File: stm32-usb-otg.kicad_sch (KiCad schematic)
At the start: 42 parts

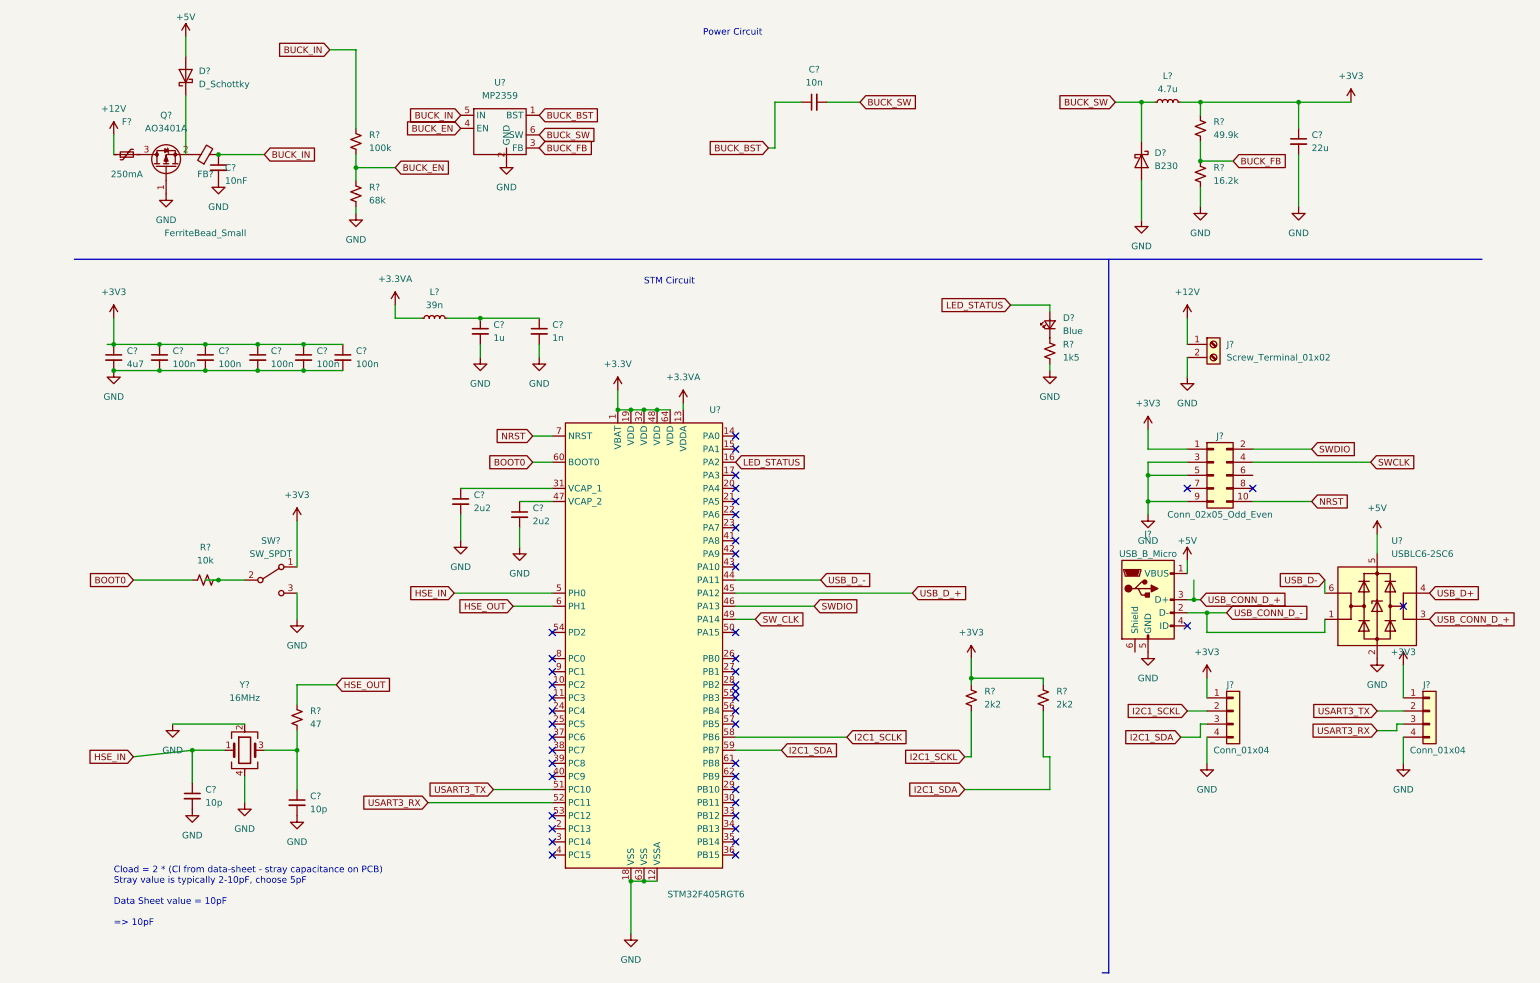
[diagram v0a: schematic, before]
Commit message: Resolving a few ERC errors with power flag based power.
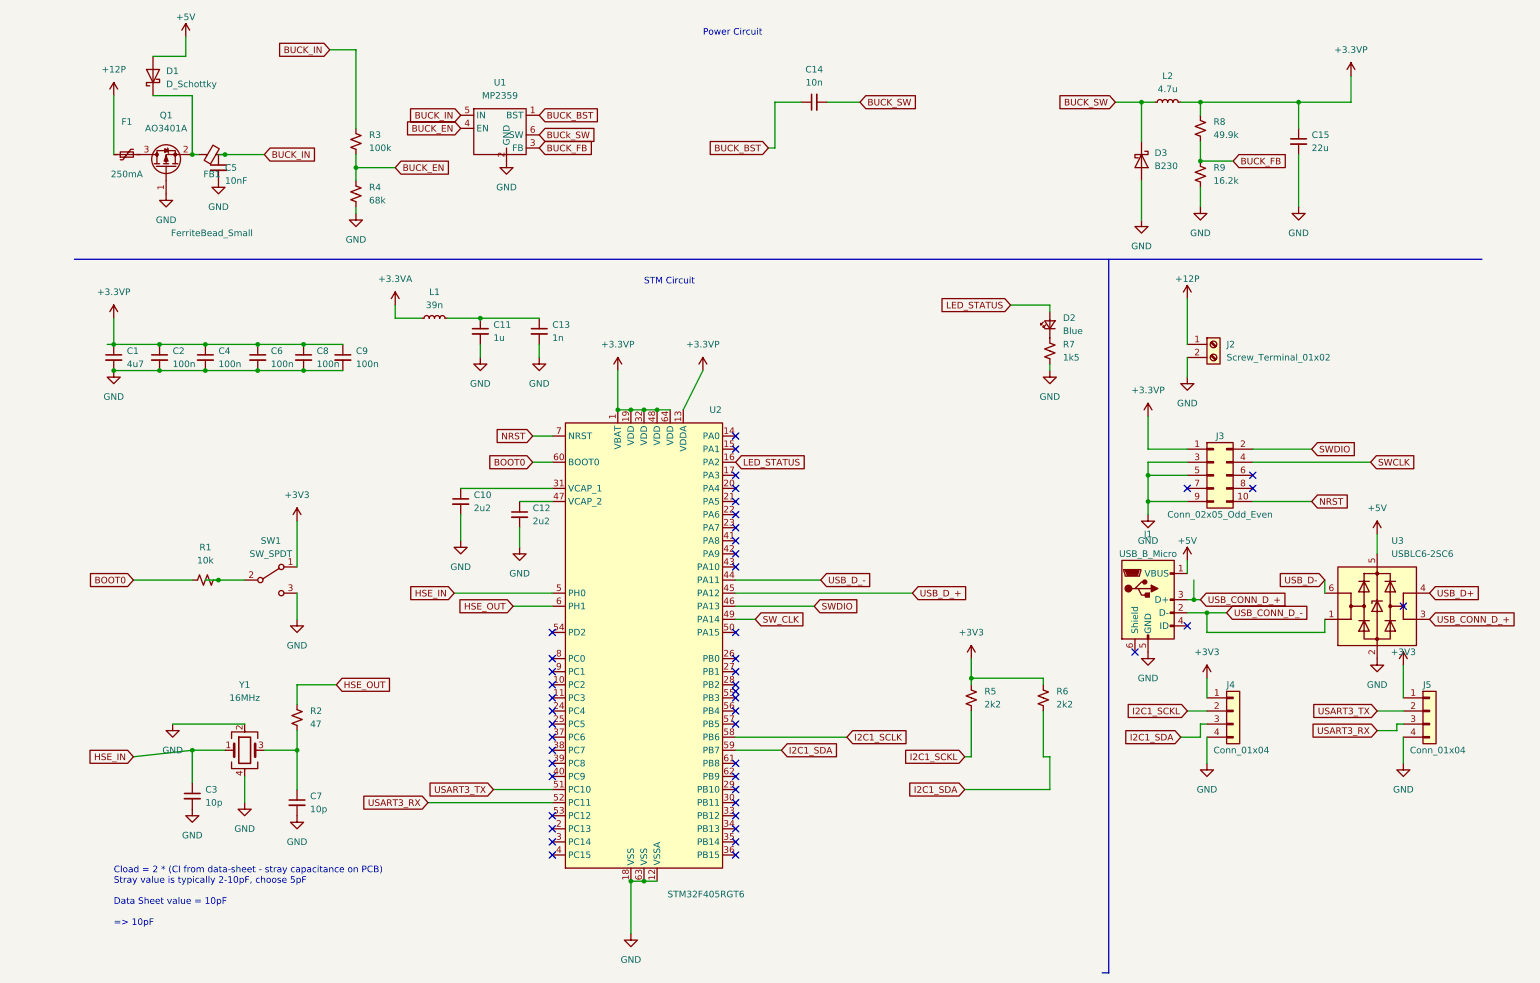
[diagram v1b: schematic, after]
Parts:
- removed D?: D_Schottky, symbol Device:D_Schottky
- added D1: D_Schottky, symbol Device:D_Schottky
- C1: renamed from C?; footprint (none) -> Capacitor_SMD:CP_Elec_3x5.3
- gave numbers to parts that had none: 40
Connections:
- net +3.3VA: no longer U2.13 (VDDA)
- net +3V3: no longer C1.1, C15.1, C2.1, C4.1, C6.1, C8.1, C9.1, J3.1 (Pin_1), L2.2, R8.1, U2.1 (VBAT), U2.19 (VDD), U2.32 (VDD), U2.48 (VDD), U2.64 (VDD)
- net +5V: now also D1.2 (A)
- net at FB1.1, Q1.2 (S): now also D1.1 (K)
- net +12V renamed +12P
- new net +3.3VP: C1.1, C15.1, C2.1, C4.1, C6.1, C8.1, C9.1, J3.1 (Pin_1), L2.2, R8.1, U2.1 (VBAT), U2.13 (VDDA), U2.19 (VDD), U2.32 (VDD), U2.48 (VDD), U2.64 (VDD)
- no-connect marks 45 -> 47
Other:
- moved on the sheet: FB1

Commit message: Solving a few ERC errors.
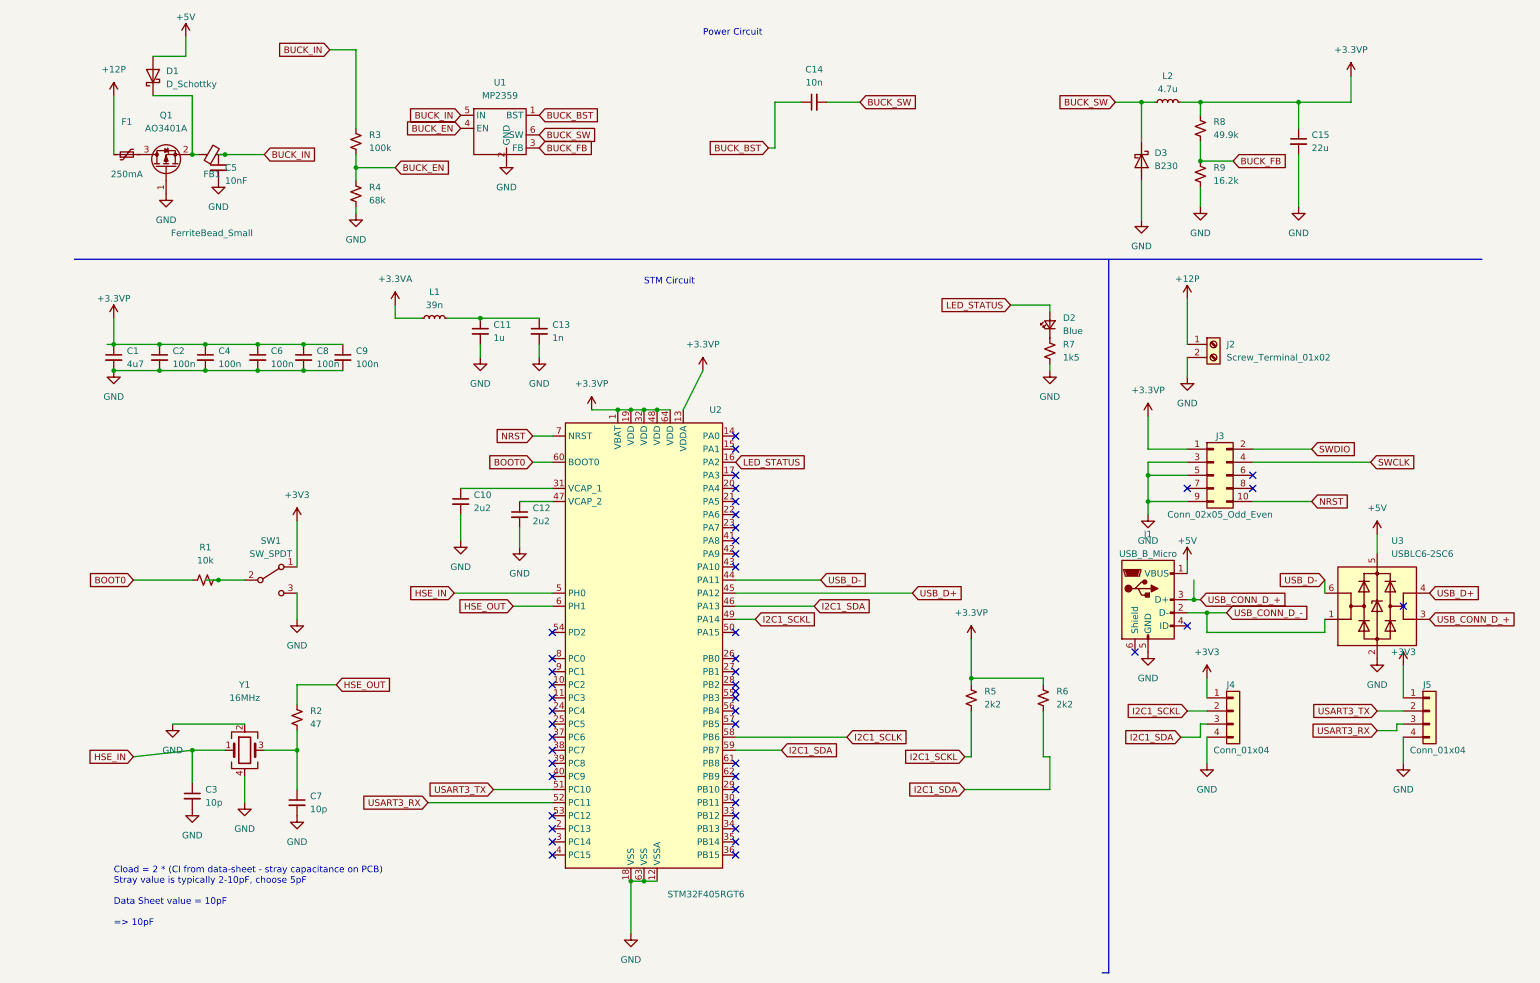
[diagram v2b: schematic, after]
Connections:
- net BUCk_SW is gone; now on net BUCK_SW: U1.6 (SW)
- net SW_CLK is gone; now on net I2C1_SCKL: U2.49 (PA14)
- net USB_D_+ is gone; now on net USB_D+: U2.45 (PA12)
- net USB_D_- is gone; now on net USB_D-: U2.44 (PA11)
- net +3.3VP: now also R5.1, R6.1
- net +3V3: no longer R5.1, R6.1
- net I2C1_SDA: now also U2.46 (PA13)
- net SWDIO: no longer U2.46 (PA13)
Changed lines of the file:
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@@
   (junction (at 231.14 40.64) (diameter 0) (color 0 0 0 0)
   )
+  (junction (at 123.19 88.9) (diameter 0) (color 0 0 0 0)
+  )
+  (junction (at 231.14 29.21) (diameter 0) (color 0 0 0 0)
+  )
+  (junction (at 220.98 106.68) (diameter 0) (color 0 0 0 0)
+  )
+  (junction (at 29.21 81.28) (diameter 0) (color 0 0 0 0)
+  )
   (junction (at 125.73 88.9) (diameter 0) (color 0 0 0 0)
   )
-  (junction (at 231.14 29.21) (diameter 0) (color 0 0 0 0)
-  )
-  (junction (at 220.98 106.68) (diameter 0) (color 0 0 0 0)
-  )
-  (junction (at 29.21 81.28) (diameter 0) (color 0 0 0 0)
-  )
   (junction (at 35.56 39.37) (diameter 0) (color 0 0 0 0)
   )
@@
   (junction (at 123.19 180.34) (diameter 0) (color 0 0 0 0)
   )
+  (junction (at 118.11 88.9) (diameter 0) (color 0 0 0 0)
+  )
   (junction (at 232.41 128.27) (diameter 0) (color 0 0 0 0)
   )
-  (junction (at 118.11 88.9) (diameter 0) (color 0 0 0 0)
-  )
   (junction (at 120.65 88.9) (diameter 0) (color 0 0 0 0)
   )
   (junction (at 186.69 140.97) (diameter 0) (color 0 0 0 0)
-  )
-  (junction (at 123.19 88.9) (diameter 0) (color 0 0 0 0)
   )
   (junction (at 35.56 154.94) (diameter 0) (color 0 0 0 0)
@@
     (stroke (width 0) (type default) (color 0 0 0 0))
   )
+  (wire (pts (xy 125.73 88.9) (xy 128.27 88.9))
+    (stroke (width 0) (type default) (color 0 0 0 0))
+  )
   (wire (pts (xy 232.41 152.4) (xy 232.41 157.48))
     (stroke (width 0) (type default) (color 0 0 0 0))
   )
-  (wire (pts (xy 118.11 81.28) (xy 118.11 88.9))
-    (stroke (width 0) (type default) (color 0 0 0 0))
-  )
   (wire (pts (xy 158.75 29.21) (xy 165.1 29.21))
     (stroke (width 0) (type default) (color 0 0 0 0))
@@
     (stroke (width 0) (type default) (color 0 0 0 0))
   )
+  (wire (pts (xy 113.03 88.9) (xy 118.11 88.9))
+    (stroke (width 0) (type default) (color 0 0 0 0))
+  )
   (wire (pts (xy 57.15 76.2) (xy 48.26 76.2))
     (stroke (width 0) (type default) (color 0 0 0 0))
@@
     (stroke (width 0) (type default) (color 0 0 0 0))
   )
-  (wire (pts (xy 128.27 88.9) (xy 125.73 88.9))
-    (stroke (width 0) (type default) (color 0 0 0 0))
-  )
-  (wire (pts (xy 125.73 88.9) (xy 123.19 88.9))
-    (stroke (width 0) (type default) (color 0 0 0 0))
-  )
   (wire (pts (xy 228.6 147.32) (xy 232.41 147.32))
     (stroke (width 0) (type default) (color 0 0 0 0))
@@
     (stroke (width 0) (type default) (color 0 0 0 0))
   )
-  (wire (pts (xy 186.69 137.16) (xy 186.69 140.97))
+  (wire (pts (xy 186.69 133.35) (xy 186.69 140.97))
+    (stroke (width 0) (type default) (color 0 0 0 0))
+  )
+  (wire (pts (xy 123.19 88.9) (xy 125.73 88.9))
     (stroke (width 0) (type default) (color 0 0 0 0))
   )
@@
     )
   )
-  (global_label "BUCk_SW" (shape input) (at 102.87 35.56 0) (fields_autoplaced)
+  (global_label "BUCK_SW" (shape input) (at 102.87 35.56 0) (fields_autoplaced)
     (effects (font (size 1.27 1.27)) (justify left))
-    (property "Intersheet References" "${INTERSHEET_REFS}" (id 0) (at 113.8102 35.4806 0)
+    (property "Intersheet References" "${INTERSHEET_REFS}" (id 0) (at 114.0521 35.4806 0)
       (effects (font (size 1.27 1.27)) (justify left) hide)
     )
@@
     )
   )
-  (global_label "USB_D_-" (shape input) (at 157.48 121.92 0) (fields_autoplaced)
+  (global_label "USB_D-" (shape input) (at 157.48 121.92 0) (fields_autoplaced)
     (effects (font (size 1.27 1.27)) (justify left))
-    (property "Intersheet References" "${INTERSHEET_REFS}" (id 0) (at 168.4807 121.8406 0)
+    (property "Intersheet References" "${INTERSHEET_REFS}" (id 0) (at 167.5131 121.8406 0)
       (effects (font (size 1.27 1.27)) (justify left) hide)
     )
@@
     )
   )
-  (global_label "SW_CLK" (shape input) (at 144.78 129.54 0) (fields_autoplaced)
+  (global_label "I2C1_SCKL" (shape input) (at 144.78 129.54 0) (fields_autoplaced)
     (effects (font (size 1.27 1.27)) (justify left))
-    (property "Intersheet References" "${INTERSHEET_REFS}" (id 0) (at 154.3898 129.4606 0)
+    (property "Intersheet References" "${INTERSHEET_REFS}" (id 0) (at 157.2321 129.4606 0)
       (effects (font (size 1.27 1.27)) (justify left) hide)
     )
@@
     )
   )
-  (global_label "SWDIO" (shape input) (at 156.21 127 0) (fields_autoplaced)
+  (global_label "I2C1_SDA" (shape input) (at 156.21 127 0) (fields_autoplaced)
     (effects (font (size 1.27 1.27)) (justify left))
-    (property "Intersheet References" "${INTERSHEET_REFS}" (id 0) (at 164.4893 126.9206 0)
+    (property "Intersheet References" "${INTERSHEET_REFS}" (id 0) (at 167.4526 126.9206 0)
       (effects (font (size 1.27 1.27)) (justify left) hide)
     )
@@
     )
   )
-  (global_label "USB_D_+" (shape input) (at 175.26 124.46 0) (fields_autoplaced)
+  (global_label "USB_D+" (shape input) (at 175.26 124.46 0) (fields_autoplaced)
     (effects (font (size 1.27 1.27)) (justify left))
-    (property "Intersheet References" "${INTERSHEET_REFS}" (id 0) (at 186.2607 124.3806 0)
+    (property "Intersheet References" "${INTERSHEET_REFS}" (id 0) (at 185.2931 124.3806 0)
       (effects (font (size 1.27 1.27)) (justify left) hide)
     )
@@
   )
   (symbol (lib_id "power:+3.3VP") (at 20.32 71.12 0) (unit 1)
-    (in_bom yes) (on_board yes) (fields_autoplaced)
+    (in_bom yes) (on_board yes)
     (property "Reference" "#PWR0107" (id 0) (at 24.13 72.39 0)
       (effects (font (size 1.27 1.27)) hide)
     )
-    (property "Value" "+3.3VP" (id 1) (at 20.32 66.04 0))
+    (property "Value" "+3.3VP" (id 1) (at 20.32 67.31 0))
     (property "Footprint" "" (id 2) (at 20.32 71.12 0)
       (effects (font (size 1.27 1.27)) hide)
     )
     (property "Datasheet" "" (id 3) (at 20.32 71.12 0)
-      (effects (font (size 1.27 1.27)) hide)
-    )
-    (pin "1")
-  )
-  (symbol (lib_id "power:+3V3") (at 186.69 137.16 0) (unit 1)
-    (in_bom yes) (on_board yes) (fields_autoplaced)
-    (property "Reference" "#PWR023" (id 0) (at 186.69 140.97 0)
-      (effects (font (size 1.27 1.27)) hide)
-    )
-    (property "Value" "+3V3" (id 1) (at 186.69 132.08 0))
-    (property "Footprint" "" (id 2) (at 186.69 137.16 0)
-      (effects (font (size 1.27 1.27)) hide)
-    )
-    (property "Datasheet" "" (id 3) (at 186.69 137.16 0)
       (effects (font (size 1.27 1.27)) hide)
     )
@@
     (pin "6")
   )
-  (symbol (lib_id "power:+3.3VP") (at 118.11 81.28 0) (unit 1)
+  (symbol (lib_id "power:+3.3VP") (at 186.69 133.35 0) (unit 1)
+    (in_bom yes) (on_board yes) (fields_autoplaced)
+    (property "Reference" "#PWR0108" (id 0) (at 190.5 134.62 0)
+      (effects (font (size 1.27 1.27)) hide)
+    )
+    (property "Value" "+3.3VP" (id 1) (at 186.69 128.27 0))
+    (property "Footprint" "" (id 2) (at 186.69 133.35 0)
+      (effects (font (size 1.27 1.27)) hide)
+    )
+    (property "Datasheet" "" (id 3) (at 186.69 133.35 0)
+      (effects (font (size 1.27 1.27)) hide)
+    )
+    (pin "1")
+  )
+  (symbol (lib_id "power:+3.3VP") (at 113.03 88.9 0) (unit 1)
     (in_bom yes) (on_board yes)
-    (property "Reference" "#PWR0102" (id 0) (at 121.92 82.55 0)
-      (effects (font (size 1.27 1.27)) hide)
-    )
-    (property "Value" "+3.3VP" (id 1) (at 118.11 76.2 0))
-    (property "Footprint" "" (id 2) (at 118.11 81.28 0)
-      (effects (font (size 1.27 1.27)) hide)
-    )
-    (property "Datasheet" "" (id 3) (at 118.11 81.28 0)
+    (property "Reference" "#PWR0102" (id 0) (at 116.84 90.17 0)
+      (effects (font (size 1.27 1.27)) hide)
+    )
+    (property "Value" "+3.3VP" (id 1) (at 113.03 83.82 0))
+    (property "Footprint" "" (id 2) (at 113.03 88.9 0)
+      (effects (font (size 1.27 1.27)) hide)
+    )
+    (property "Datasheet" "" (id 3) (at 113.03 88.9 0)
       (effects (font (size 1.27 1.27)) hide)
     )
@@
       (reference "#PWR021") (unit 1) (value "GND") (footprint "")
     )
-    (path "/09af7b8a-d581-478f-8091-49787124dcd5"
-      (reference "#PWR023") (unit 1) (value "+3V3") (footprint "")
-    )
     (path "/a6164d79-af78-4616-88f6-fd1b2984b009"
       (reference "#PWR024") (unit 1) (value "GND") (footprint "")
@@
       (reference "#PWR0107") (unit 1) (value "+3.3VP") (footprint "")
     )
+    (path "/6d66fb2a-f62f-4693-b8d3-188df268bdd9"
+      (reference "#PWR0108") (unit 1) (value "+3.3VP") (footprint "")
+    )
     (path "/5483ad66-6e3b-4569-90b8-77d47f276440"
